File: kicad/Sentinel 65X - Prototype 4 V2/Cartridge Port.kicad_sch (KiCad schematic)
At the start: 13 parts, among them J6 2x32 2.54mm Card Edge Connect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

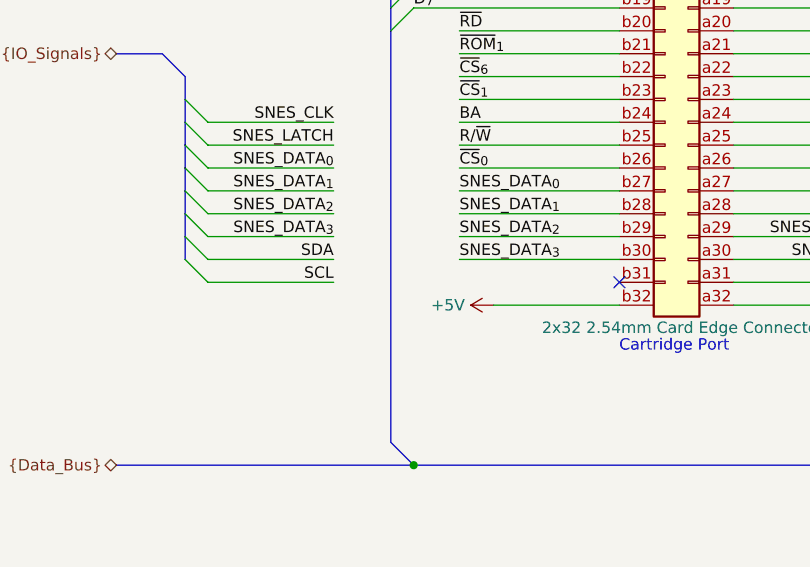
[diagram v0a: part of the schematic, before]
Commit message: Updated prototype 4V2 schematic
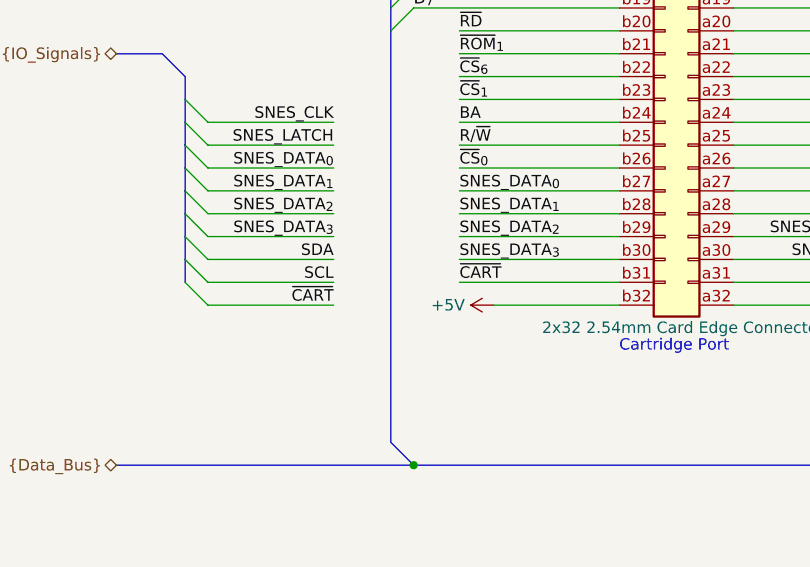
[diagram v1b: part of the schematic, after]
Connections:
- net ~{CART}: now reaches J6.b31 (Pin_b31)
- no-connect marks 7 -> 6
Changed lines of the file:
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@@
 		(at 212.09 129.54)
 	)
-	(no_connect
-		(at 105.41 111.76)
-	)
 	(bus_entry
 		(at 193.04 96.52)
@@
 	)
 	(bus_entry
+		(at 57.15 111.76)
+		(size 2.54 2.54)
+		(stroke
+			(width 0)
+			(type default)
+		)
+	)
+	(bus_entry
 		(at 193.04 30.48)
 		(size 2.54 2.54)
@@
 		)
 	)
+	(wire
+		(pts
+			(xy 59.69 114.3) (xy 73.66 114.3)
+		)
+		(stroke
+			(width 0)
+			(type default)
+		)
+	)
 	(bus
 		(pts
@@
 		)
 	)
+	(bus
+		(pts
+			(xy 57.15 109.22) (xy 57.15 111.76)
+		)
+		(stroke
+			(width 0)
+			(type default)
+		)
+	)
 	(wire
 		(pts
@@
 		)
 	)
+	(wire
+		(pts
+			(xy 105.41 111.76) (xy 87.63 111.76)
+		)
+		(stroke
+			(width 0)
+			(type default)
+		)
+	)
 	(bus
 		(pts
@@
 		)
 	)
+	(label "~{CART}"
+		(at 73.66 114.3 180)
+		(fields_autoplaced yes)
+		(effects
+			(font
+				(size 1.27 1.27)
+			)
+			(justify right bottom)
+		)
+	)
 	(label "~{CS}_{7}"
 		(at 73.66 62.23 180)
@@
 		(fields_autoplaced yes)
 		(effects
+			(font
+				(size 1.27 1.27)
+			)
+			(justify left bottom)
+		)
+	)
+	(label "~{CART}"
+		(at 87.63 111.76 0)
+		(fields_autoplaced yes)
+		(effects
